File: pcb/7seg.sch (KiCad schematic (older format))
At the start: 28 parts, among them Q10 2SC1815, Q11 2SC1815, Q12 2SC1815, Q13 2SC1815, Q14 2SC1815, Q9 2SC1815, U7 7seg-2digit-ca, U8 7seg-2digit-ca, U9 7seg-2digit-ca

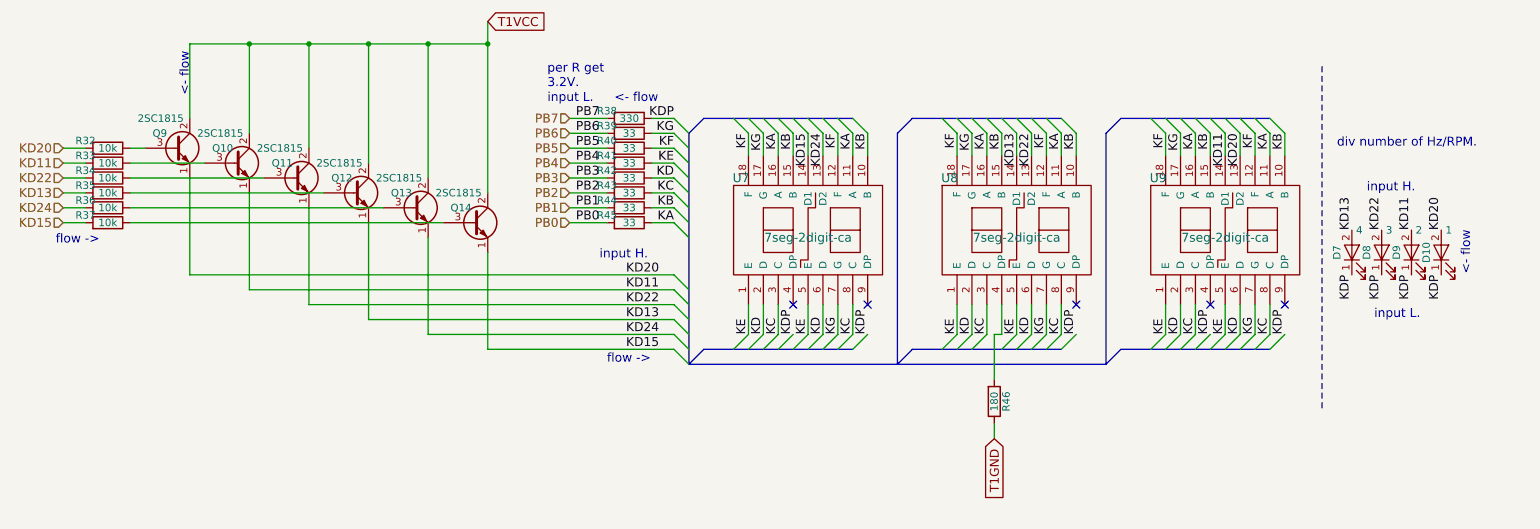
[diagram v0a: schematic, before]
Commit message: ERC 走らせたら，いくつか error を指摘されたので修正。
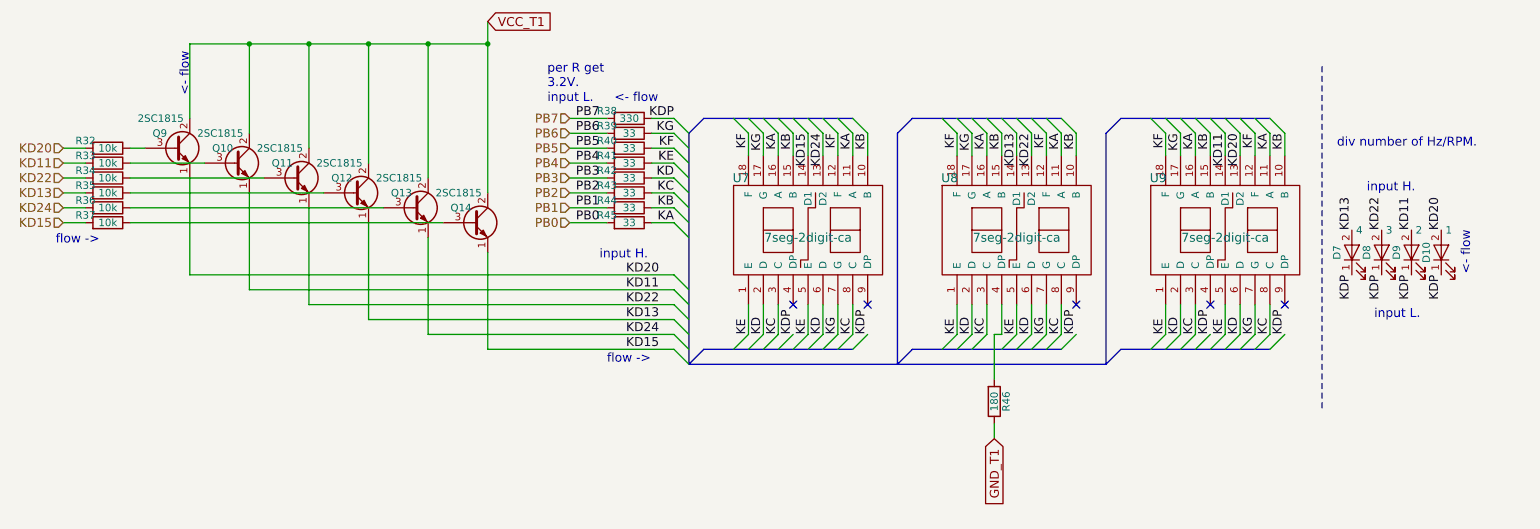
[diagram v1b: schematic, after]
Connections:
- net T1GND renamed GND_T1
- net T1VCC renamed VCC_T1
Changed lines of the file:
@@
 $EndComp
 Text GLabel 7100 4600 3    60   Input ~ 0
-T1GND
+GND_T1
 $Comp
 L 2SC1815 Q9
@@
 <- flow
 Text GLabel 3700 1800 2    60   Input ~ 0
-T1VCC
+VCC_T1
 Wire Wire Line
 	3300 3900 4950 3900

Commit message: LED に関してのCvPcbをやり直した。
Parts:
- D10, D7, D8, D9: footprint LEDs:LED_D5.0mm -> LED_THT:LED_D5.0mm
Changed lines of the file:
@@
 F 0 "D8" H 9700 3450 50  0000 C CNN
 F 1 "3" V 9850 3300 50  0000 C CNN
-F 2 "LEDs:LED_D5.0mm" H 9700 3350 50  0001 C CNN
+F 2 "LED_THT:LED_D5.0mm" H 9700 3350 50  0001 C CNN
 F 3 "" H 9700 3350 50  0001 C CNN
 	1    9700 3350
@@
 F 0 "D9" H 9900 3450 50  0000 C CNN
 F 1 "2" V 10050 3300 50  0000 C CNN
-F 2 "LEDs:LED_D5.0mm" H 9900 3350 50  0001 C CNN
+F 2 "LED_THT:LED_D5.0mm" H 9900 3350 50  0001 C CNN
 F 3 "" H 9900 3350 50  0001 C CNN
 	1    9900 3350
@@
 F 0 "D7" H 9500 3450 50  0000 C CNN
 F 1 "4" V 9650 3300 50  0000 C CNN
-F 2 "LEDs:LED_D5.0mm" H 9500 3350 50  0001 C CNN
+F 2 "LED_THT:LED_D5.0mm" H 9500 3350 50  0001 C CNN
 F 3 "" H 9500 3350 50  0001 C CNN
 	1    9500 3350
@@
 F 0 "D10" H 10100 3450 50  0000 C CNN
 F 1 "1" V 10250 3300 50  0000 C CNN
-F 2 "LEDs:LED_D5.0mm" H 10100 3350 50  0001 C CNN
+F 2 "LED_THT:LED_D5.0mm" H 10100 3350 50  0001 C CNN
 F 3 "" H 10100 3350 50  0001 C CNN
 	1    10100 3350

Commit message: KiCad 5.0 change some files.
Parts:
- D10, D7, D8, D9: symbol LED -> freq-counter-rescue:LED
- Q10, Q11, Q12, Q13, Q14, Q9: symbol 2SC1815 -> freq-counter-rescue:2SC1815
- R32, R33, R34, R35, R36, R37, R38, R39, R40, R41, R42, R43, R44, R45, R46: symbol R -> freq-counter-rescue:R
- U7, U8, U9: symbol 7seg-2digit-ca -> freq-counter-rescue:7seg-2digit-ca
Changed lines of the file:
@@
-EESchema Schematic File Version 2
-LIBS:7seg-4digit
-LIBS:power
-LIBS:device
-LIBS:switches
-LIBS:relays
-LIBS:motors
-LIBS:transistors
-LIBS:conn
-LIBS:linear
-LIBS:regul
-LIBS:74xx
-LIBS:cmos4000
-LIBS:adc-dac
-LIBS:memory
-LIBS:xilinx
-LIBS:microcontrollers
-LIBS:dsp
-LIBS:microchip
-LIBS:analog_switches
-LIBS:motorola
-LIBS:texas
-LIBS:intel
-LIBS:audio
-LIBS:interface
-LIBS:digital-audio
-LIBS:philips
-LIBS:display
-LIBS:cypress
-LIBS:siliconi
-LIBS:opto
-LIBS:atmel
-LIBS:contrib
-LIBS:valves
+EESchema Schematic File Version 4
 LIBS:freq-counter-cache
-EELAYER 25 0
+EELAYER 26 0
 EELAYER END
 $Descr A4 11693 8268
@@
 $EndDescr
 $Comp
-L 7seg-2digit-ca U7
+L freq-counter-rescue:7seg-2digit-ca U7
 U 1 1 5A12333C
 P 5850 3200
@@
 	5050 4100 5150 4000
 $Comp
-L R R39
+L freq-counter-rescue:R R39
 U 1 1 5A123365
 P 4650 2550
@@
 $EndComp
 $Comp
-L R R40
+L freq-counter-rescue:R R40
 U 1 1 5A12336C
 P 4650 2650
@@
 $EndComp
 $Comp
-L R R41
+L freq-counter-rescue:R R41
 U 1 1 5A123373
 P 4650 2750
@@
 $EndComp
 $Comp
-L R R42
+L freq-counter-rescue:R R42
 U 1 1 5A12337A
 P 4650 2850
@@
 $EndComp
 $Comp
-L R R43
+L freq-counter-rescue:R R43
 U 1 1 5A123381
 P 4650 2950
@@
 $EndComp
 $Comp
-L R R44
+L freq-counter-rescue:R R44
 U 1 1 5A123388
 P 4650 3050
@@
 $EndComp
 $Comp
-L R R45
+L freq-counter-rescue:R R45
 U 1 1 5A12338F
 P 4650 3150
@@
 	5050 3250 4950 3150
 $Comp
-L 7seg-2digit-ca U8
+L freq-counter-rescue:7seg-2digit-ca U8
 U 1 1 5A1233A6
 P 7250 3200
@@
 	6450 4100 6550 4000
 $Comp
-L 7seg-2digit-ca U9
+L freq-counter-rescue:7seg-2digit-ca U9
 U 1 1 5A1233CF
 P 8650 3200
@@
 NoConn ~ 7650 3700
 $Comp
-L LED D8
+L freq-counter-rescue:LED D8
 U 1 1 5A123402
 P 9700 3350
@@
 $EndComp
 $Comp
-L LED D9
+L freq-counter-rescue:LED D9
 U 1 1 5A123409
 P 9900 3350
@@
 $EndComp
 $Comp
-L LED D7
+L freq-counter-rescue:LED D7
 U 1 1 5A123410
 P 9500 3350
@@
 $EndComp
 $Comp
-L LED D10
+L freq-counter-rescue:LED D10
 U 1 1 5A123417
 P 10100 3350
@@
 KDP
 $Comp
-L R R46
+L freq-counter-rescue:R R46
 U 1 1 5A123422
 P 7100 4350
@@
 KD15
 $Comp
-L R R38
+L freq-counter-rescue:R R38
 U 1 1 5A129408
 P 4650 2450
@@
 GND_T1
 $Comp
-L 2SC1815 Q9
+L freq-counter-rescue:2SC1815 Q9
 U 1 1 5A107034
 P 1600 2650
@@
 $EndComp
 $Comp
-L R R32
+L freq-counter-rescue:R R32
 U 1 1 5A1075D9
 P 1150 2650
@@
 $EndComp
 $Comp
-L R R33
+L freq-counter-rescue:R R33
 U 1 1 5A107776
 P 1150 2750
@@
 $EndComp
 $Comp
-L R R34
+L freq-counter-rescue:R R34
 U 1 1 5A1077BF
 P 1150 2850
@@
 $EndComp
 $Comp
-L R R35
+L freq-counter-rescue:R R35
 U 1 1 5A10780B
 P 1150 2950
@@
 $EndComp
 $Comp
-L R R36
+L freq-counter-rescue:R R36
 U 1 1 5A10785A
 P 1150 3050
@@
 $EndComp
 $Comp
-L R R37
+L freq-counter-rescue:R R37
 U 1 1 5A1078AC
 P 1150 3150
@@
 $EndComp
 $Comp
-L 2SC1815 Q10
+L freq-counter-rescue:2SC1815 Q10
 U 1 1 5A107D1F
 P 2000 2750
@@
 $EndComp
 $Comp
-L 2SC1815 Q11
+L freq-counter-rescue:2SC1815 Q11
 U 1 1 5A107D99
 P 2400 2850
@@
 $EndComp
 $Comp
-L 2SC1815 Q12
+L freq-counter-rescue:2SC1815 Q12
 U 1 1 5A107E06
 P 2800 2950
@@
 $EndComp
 $Comp
-L 2SC1815 Q13
+L freq-counter-rescue:2SC1815 Q13
 U 1 1 5A107E72
 P 3200 3050
@@
 $EndComp
 $Comp
-L 2SC1815 Q14
+L freq-counter-rescue:2SC1815 Q14
 U 1 1 5A107FF8
 P 3600 3150
